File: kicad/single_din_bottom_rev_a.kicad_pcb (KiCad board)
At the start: 2 copper layers, 86 x 14 mm, 9 parts, among them J1 Conn_01x04, J2 Conn_01x04, J3 Conn_01x04, J4 Conn_01x04, U1 R-78B3.3-1.0 (Recom)

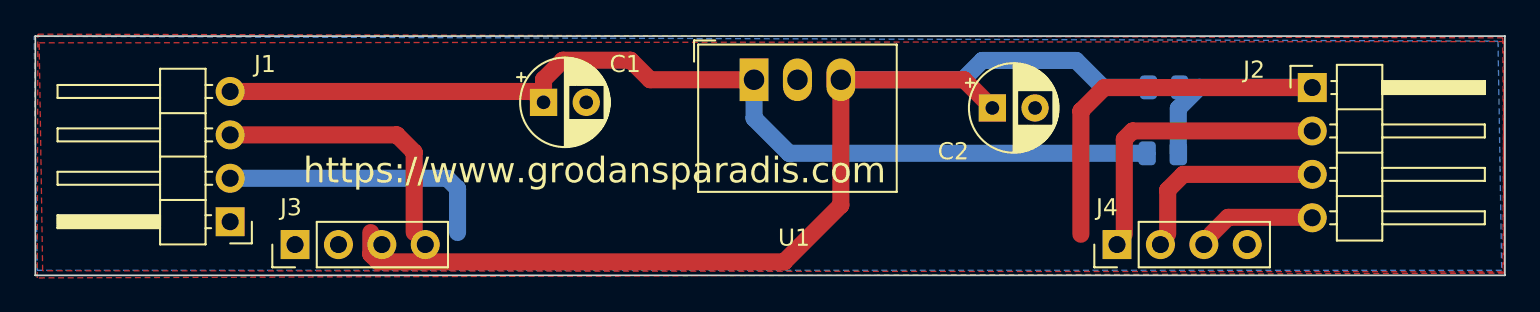
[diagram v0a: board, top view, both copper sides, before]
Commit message: Fixed board to board connectors
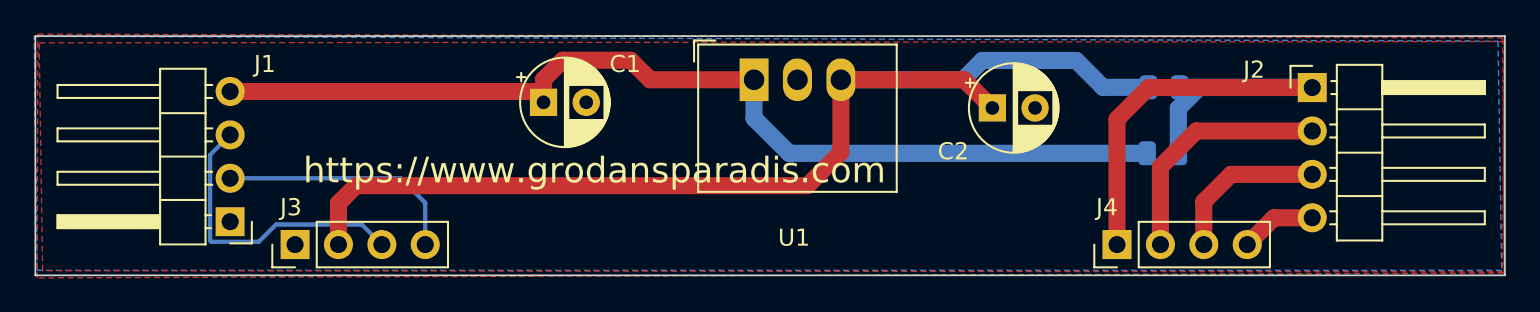
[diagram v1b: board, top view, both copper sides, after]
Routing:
- net /IO2: track 16.8 -> 14.3 mm
- net /IO3: track 11.4 -> 9.52 mm
- net /IO4: track 6.34 -> 4.45 mm
- net /IO1: track 33.5 -> 31.7 mm
- net Net-(J1-Pad3): track 15.9 -> 17.7 mm
- net Net-(J1-Pad2): track 16.1 -> 14.5 mm

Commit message: Added cutots
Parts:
- J1, J2: footprint Connector_PinHeader_2.54mm:PinHeader_1x04_P2.54mm_Horizontal -> Connector_PinHeader_2.54mm:PinHeader_1x04_P2.54mm_Vertical
- moved J4 8.91 mm to (84.4, 177.9)
- moved J3 8.68 mm to (53.9, 177.6)
- moved J1 3.58 mm to (37.8, 176.9)
- moved J2 3.07 mm to (107.8, 169.1)
- moved R1 2.86 mm to (93.2, 169.0)
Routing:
- net /IO1: track 31.7 -> 46.4 mm
- net /IO4: track 4.45 -> 16.8 mm
- net Net-(J1-Pad2): track 14.5 -> 26.3 mm
- net /Vout: track 66.0 -> 54.4 mm, vias 0 -> 1
- net /IO3: track 9.52 -> 20.1 mm
- net /IO2: track 14.3 -> 24.8 mm
- net Net-(J1-Pad3): track 17.7 -> 25.5 mm
- net /Vin: track 59.3 -> 64.1 mm
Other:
- outline, holes or cut-outs redrawn
- board text added: "DIN M1 Base board rev B"
- board text removed: "DIN M1 Base board rev A"
